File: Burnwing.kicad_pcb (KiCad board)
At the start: 2 copper layers, 50.8 x 22.9 mm, 61 parts, among them J1 Conn_01x06_MountingPin, J2 PinHeader_1x02_P1.00mm_Vertic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, Q1 AONR21307, Q2 NCV8402ADDR2G, X1 USB Type C, X2 HUSB238

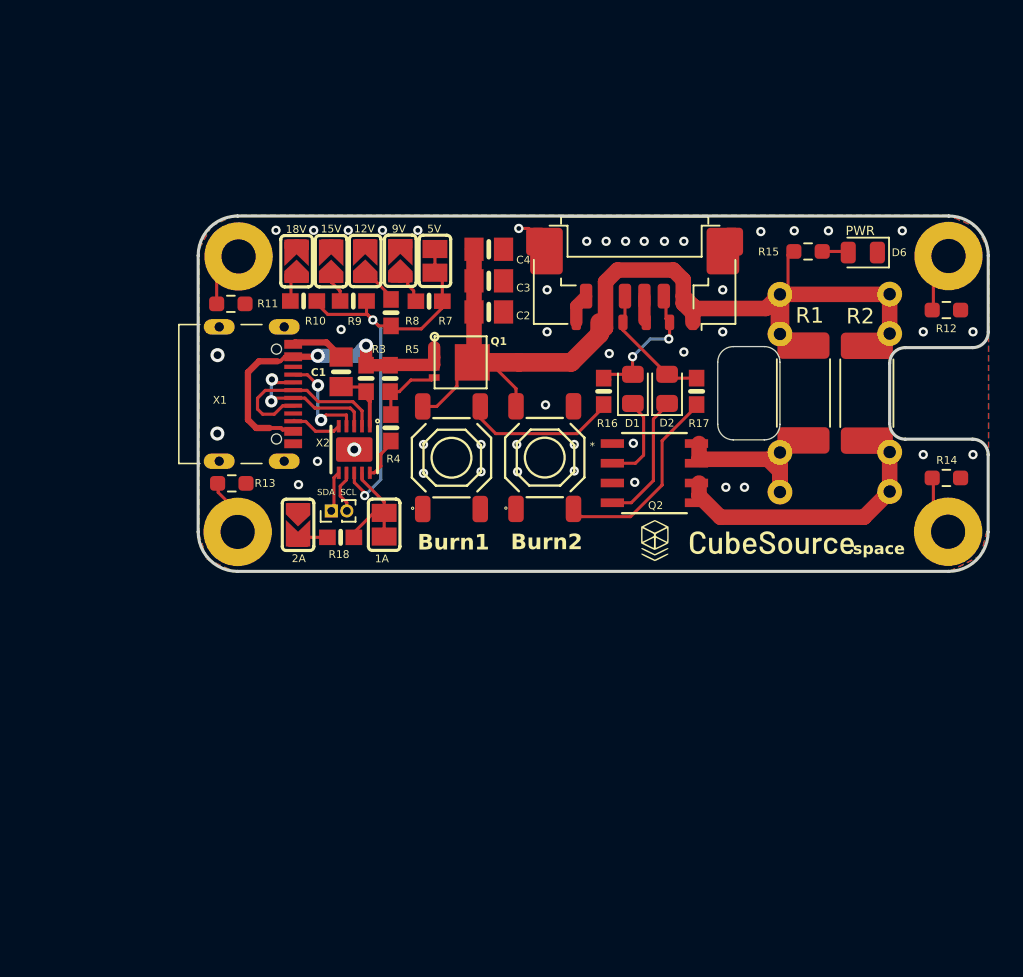
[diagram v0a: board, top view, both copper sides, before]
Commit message: Reworked the layout
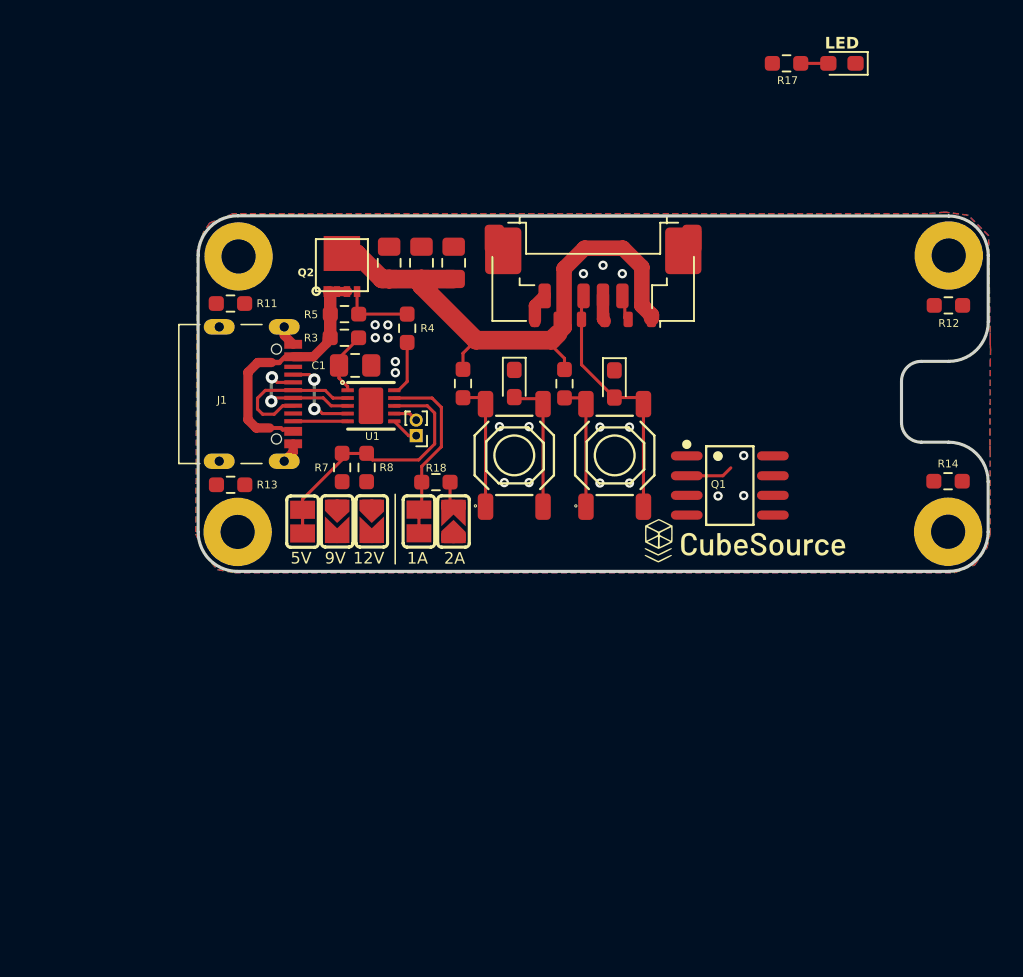
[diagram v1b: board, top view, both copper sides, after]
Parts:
- removed 15V, 18V: , Library:SOLDERJUMPER_ARROW_NOPASTE
- removed D6: LED_RED_IN1, Library:LED_0805_2012Metric
- removed H2: MountingHole_Pad, Library:MountingHole_2.2mm_M2_Pad
- removed the Q2 at (106.9, 96.6)
- removed R1: 4.7, Library:AxialBurnResistor
- removed R16: 510, Library:0603-NO
- removed the R17 at (109.6, 91.3)
- removed R2: 4.7, Library:AxialBurnResistor_No_Cutout
- removed REF** (x2): R_2512_6332Metric_Pad1.40x3.35mm_HandSolder, Library:R_2512_6332Metric_Pad1.40x3.35mm_HandSolder
- added ?: MountingHole_2.2mm_M2_Pad, MountingHole:MountingHole_2.2mm_M2_Pad, F.Cu at (125.8, 82.6)
- added D3: LED, LED_SMD:LED_0603_1608Metric_Pad1.05x0.95mm_HandSolder, F.Cu at (119.0, 70.2)
- added Q1: NCV8402ADDR2G, EasyEDA:SOIC-8_L4.9-W3.9-P1.27-LS6.0-BL, F.Cu at (111.8, 97.4)
- Burn1, Burn2: footprint Library:SW-SMD_4P-L5.1-W5.1-P3.70-LS6.5-TL-2 -> PCM_JLCPCB:SW-SMD_4P-L5.1-W5.1-P3.70-LS6.5-TL-2
- C1, C2, C3, C4: footprint Library:0805-NO -> Capacitor_SMD:C_0805_2012Metric_Pad1.18x1.45mm_HandSolder
- D1: value LED_RED_IN1 -> LED; footprint Library:LED_0805_2012Metric -> LED_SMD:LED_0603_1608Metric_Pad1.05x0.95mm_HandSolder
- D2: value LED_RED_IN2 -> LED; footprint Library:LED_0805_2012Metric -> LED_SMD:LED_0603_1608Metric_Pad1.05x0.95mm_HandSolder
- H1, H3, H4: footprint Library:MountingHole_2.2mm_M2_Pad -> MountingHole:MountingHole_2.2mm_M2_Pad
- J2: renamed from J1; footprint Library:Molex_PicoBlade_53261-0671_1x06-1MP_P1.25mm_Horizontal -> Connector_Molex:Molex_PicoBlade_53261-0671_1x06-1MP_P1.25mm_Horizontal
- J3: renamed from J2; value PinHeader_1x02_P1.00mm_Vertical -> Conn_01x02_Pin; footprint Library:PinHeader_1x02_P1.00mm_Vertical -> Connector_PinHeader_1.00mm:PinHeader_1x02_P1.00mm_Vertical
- R10: value 18K -> 750; footprint Library:0603-NO -> Resistor_SMD:R_0603_1608Metric_Pad0.98x0.95mm_HandSolder
- R11, R12, R13, R14: footprint Library:R_0603_1608Metric_Pad0.98x0.95mm_HandSolder -> Resistor_SMD:R_0603_1608Metric_Pad0.98x0.95mm_HandSolder
- R17: renamed from R15; value 750 -> 5.1K; footprint Library:R_0603_1608Metric_Pad0.98x0.95mm_HandSolder -> Resistor_SMD:R_0603_1608Metric_Pad0.98x0.95mm_HandSolder
- R18, R4, R5, R7, R8: footprint Library:0603-NO -> Resistor_SMD:R_0603_1608Metric_Pad0.98x0.95mm_HandSolder
- R3: value 10 ohm -> 10; footprint Library:0603-NO -> Resistor_SMD:R_0603_1608Metric_Pad0.98x0.95mm_HandSolder
- R9: value 14K -> 750; footprint Library:0603-NO -> Resistor_SMD:R_0603_1608Metric_Pad0.98x0.95mm_HandSolder
- moved 5V 18.8 mm to (84.3, 99.7), turned to -90 degrees
- moved R10 17.6 mm to (101.1, 90.8), turned to -90 degrees
- moved 9V 17.3 mm to (86.5, 99.7), turned to -90 degrees
- moved 12V 16.8 mm to (88.7, 99.7), turned to -90 degrees
- moved R17 12.2 mm to (115.4, 70.2)
- moved R7 12.1 mm to (86.8, 96.2), turned to 90 degrees
- moved R8 10.1 mm to (88.4, 96.2), turned to 90 degrees
- moved 2A 10.0 mm to (94.0, 99.7), turned to 90 degrees
- moved D2 9.84 mm to (97.9, 90.8), turned to -90 degrees
- moved Q2 9.51 mm to (86.8, 83.5), turned to 90 degrees
- moved R9 8.83 mm to (94.6, 90.8), turned to -90 degrees
- moved J3 7.30 mm to (91.6, 94.2), turned to 180 degrees
- moved R18 7.08 mm to (92.8, 97.2), turned to 180 degrees
- moved R4 6.49 mm to (91.0, 87.3)
- moved C4 6.47 mm to (89.8, 83.1), turned to 90 degrees
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- renumbered X1 to J1, Q1 to Q2, X2 to U1
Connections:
- net CC1 renamed /CC1
- net CC2 renamed /CC2
- net D+ renamed /D+
- net D- renamed /D-
- net SCL renamed /SCL
- net SDA renamed /SDA
- net VBUS renamed /VBUS
- 5V pad 1: N$3 -> Net-(U1-VSET)
- Burn1 pad 1: (no net) -> Net-(Burn1-B)
- Burn1 pad 2: VOUT -> Net-(Burn1-B)
- Burn1 pad 3: (no net) -> BURN_CTRL_1
- Burn2 pad 1: (no net) -> Net-(Burn2-B)
- Burn2 pad 2: VOUT -> Net-(Burn2-B)
- Burn2 pad 4: (no net) -> BURN_CTRL_2
- C2 pad 1: VOUT -> VDC
- C3 pad 1: VOUT -> VDC
- C4 pad 1: VOUT -> VDC
- D1 pad 1: /GATE1 -> Net-(D1-K)
- D1 pad 2: BURN_CTRL_1 -> BURN_CTRL_2
- D2 pad 1: /GATE2 -> GND
- D2 pad 2: BURN_CTRL_2 -> BURN_CTRL_1
- J1 pad A8: (no net) -> unconnected-(J1-SBU1-PadA8)
- J1 pad B8: (no net) -> unconnected-(J1-SBU2-PadB8)
- J2 pad 1: VOUT -> VDC
- J2 pad 5: VOUT -> VDC
- Q2 pad 5678: VOUT -> VDC
- R10 pad 1: N$8 -> VDC
- R10 pad 2: N$3 -> Net-(Burn2-B)
- R12 pad 1: Net-(H2-Pad1) -> Net-(H3-Pad1)
- R13 pad 1: Net-(H3-Pad1) -> Net-(H2-Pad1)
- R17 pad 1: VOUT -> VDC
- R17 pad 2: VOUT -> Net-(D3-A)
- R7 pad 2: N$3 -> Net-(U1-VSET)
- R8 pad 2: N$3 -> Net-(U1-VSET)
- R9 pad 1: N$7 -> VDC
- R9 pad 2: N$3 -> Net-(Burn1-B)
- U1 pad 8: N$3 -> Net-(U1-VSET)
- p pad 1: VOUT -> VDC
- p pad 5: VOUT -> VDC
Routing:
- net VOUT: track 66.2 -> 0.00 mm
- net VDC: track 0.00 -> 40.8 mm
- net N$3: track 26.9 -> 0.00 mm, vias 2 -> 0
- net Net-(R2-Pad2): track 16.9 -> 0.00 mm
- net Net-(U1-VSET): track 0.00 -> 16.1 mm
- net Net-(R1-Pad2): track 14.0 -> 0.00 mm
- net /GATE2: track 8.56 -> 0.00 mm
- net Net-(Burn1-B): track 0.00 -> 8.39 mm
- net Net-(Burn2-B): track 0.00 -> 8.15 mm
- net BURN_CTRL_1: track 19.9 -> 12.5 mm, vias 2 -> 0
- net /GATE1: track 5.83 -> 0.00 mm
- net BURN_CTRL_2: track 20.9 -> 16.1 mm
- net Net-(U1-ISET): track 5.70 -> 10.5 mm
- net Net-(H3-Pad1): track 4.63 -> 0.00 mm
- net /VBUS: track 21.6 -> 17.0 mm, vias 2 -> 0
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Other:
- outline, holes or cut-outs redrawn
- board text removed: "PWR"

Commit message: Layout completed
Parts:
- removed ?: MountingHole_2.2mm_M2_Pad, MountingHole:MountingHole_2.2mm_M2_Pad
- added H2: MountingHole_Pad, MountingHole:MountingHole_2.2mm_M2_Pad, F.Cu at (125.8, 82.6)
- added R1: 4.7, Library:AxialBurnResistor, F.Cu at (116.4, 91.4)
- added R2: 4.7, Library:AxialBurnResistor_No_Cutout, F.Cu at (123.4, 91.4)
- added REF**: R_2512_6332Metric_Pad1.40x3.35mm_HandSolder, Library:R_2512_6332Metric_Pad1.40x3.35mm_HandSolder, F.Cu at (122.0, 91.4)
- added REF**: R_2512_6332Metric_Pad1.40x3.35mm_HandSolder, Library:R_2512_6332Metric_Pad1.40x3.35mm_HandSolder, F.Cu at (118.1, 91.4)
- D3: value LED -> PWR
- moved D3 12.4 mm to (121.0, 82.5)
- moved R17 12.4 mm to (117.5, 82.5)
- moved Q1 4.95 mm to (109.7, 92.9), turned to 180 degrees
- moved .space 2.53 mm to (114.8, 100.8)
- moved R12 0.89 mm to (125.8, 86.7), turned to -90 degrees
- moved R7 0.89 mm to (87.7, 96.2)
- moved R8 0.86 mm to (89.2, 96.2)
- moved R14 0.84 mm to (125.8, 96.3), turned to 90 degrees
- moved 1A 0.36 mm to (91.4, 99.7)
- moved Burn1 0.33 mm to (97.6, 95.4)
- moved D2 0.33 mm to (97.6, 90.8)
- moved R9 0.33 mm to (94.3, 90.8)
- moved R18 0.26 mm to (92.6, 97.2)
- moved R10 0.24 mm to (100.9, 90.8)
- moved 5V 0.23 mm to (84.0, 99.7)
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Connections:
- D1 pad 1: Net-(D1-K) -> GND
- R12 pad 1: Net-(H3-Pad1) -> Net-(H2-Pad1)
- R13 pad 1: Net-(H2-Pad1) -> Net-(H3-Pad1)
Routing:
- net BURN_CTRL_1: track 12.5 -> 36.5 mm
- net VDC: track 40.8 -> 64.6 mm
- net Net-(Q1-D2-Pad5): track 0.00 -> 21.6 mm
- net Net-(Q1-D1-Pad7): track 0.00 -> 10.8 mm
- net BURN_CTRL_2: track 16.1 -> 12.5 mm
- net Net-(H2-Pad1): track 0.00 -> 3.16 mm
- net Net-(H4-Pad1): track 0.00 -> 2.97 mm
- net Net-(U1-VSET): track 16.1 -> 14.1 mm
- net Net-(H3-Pad1): track 0.00 -> 1.67 mm
- net Net-(9V1-Pad1): track 0.00 -> 1.65 mm
- net Net-(H1-Pad1): track 0.00 -> 1.59 mm
- net Net-(12V1-Pad1): track 0.00 -> 1.56 mm
- net Net-(Burn1-A): track 8.39 -> 7.29 mm
- net Net-(U1-VIN): track 4.05 -> 3.33 mm
- net Net-(Burn2-A): track 8.15 -> 8.72 mm
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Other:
- outline, holes or cut-outs redrawn

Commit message: Cleaned schematic a bit
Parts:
- renumbered D2 to D1, D1 to D2
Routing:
- net BURN_CTRL_2: track 12.5 -> 11.9 mm
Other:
- outline, holes or cut-outs redrawn

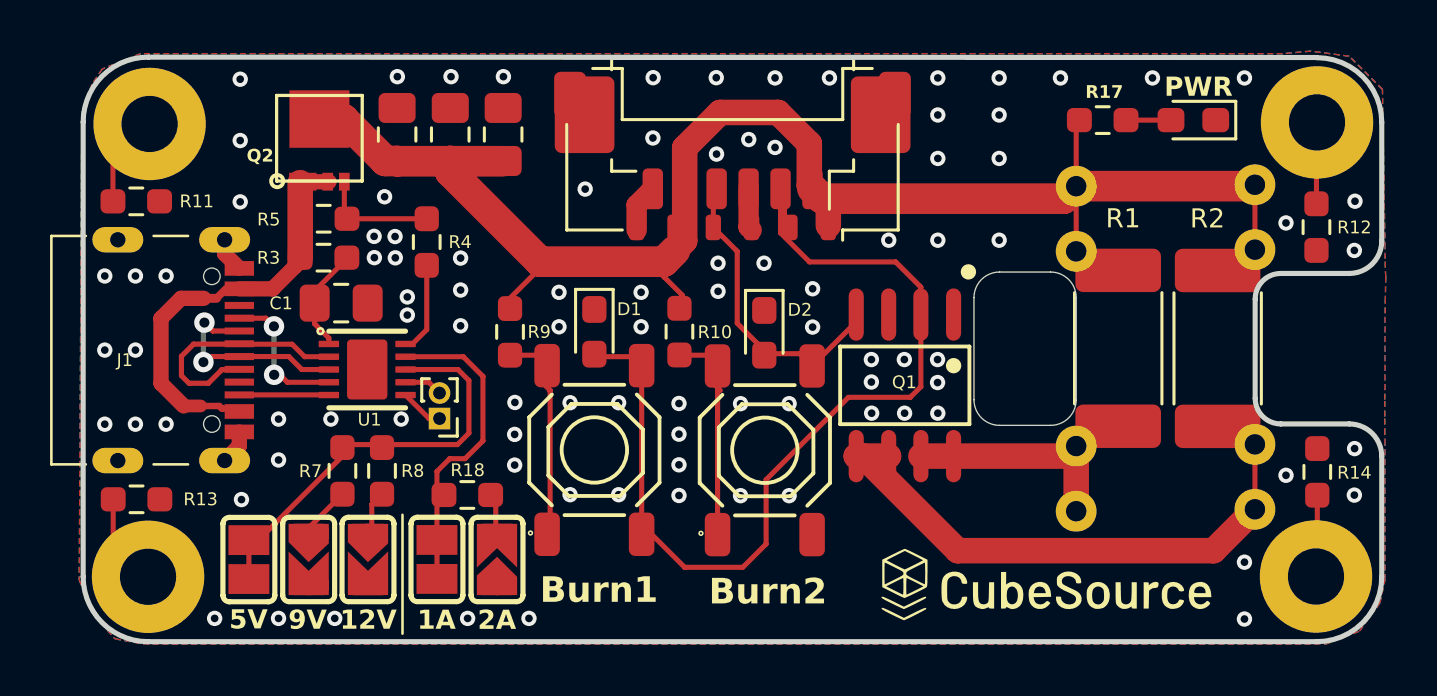
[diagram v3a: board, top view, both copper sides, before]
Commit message: Reworked usb power and cleaned up layout
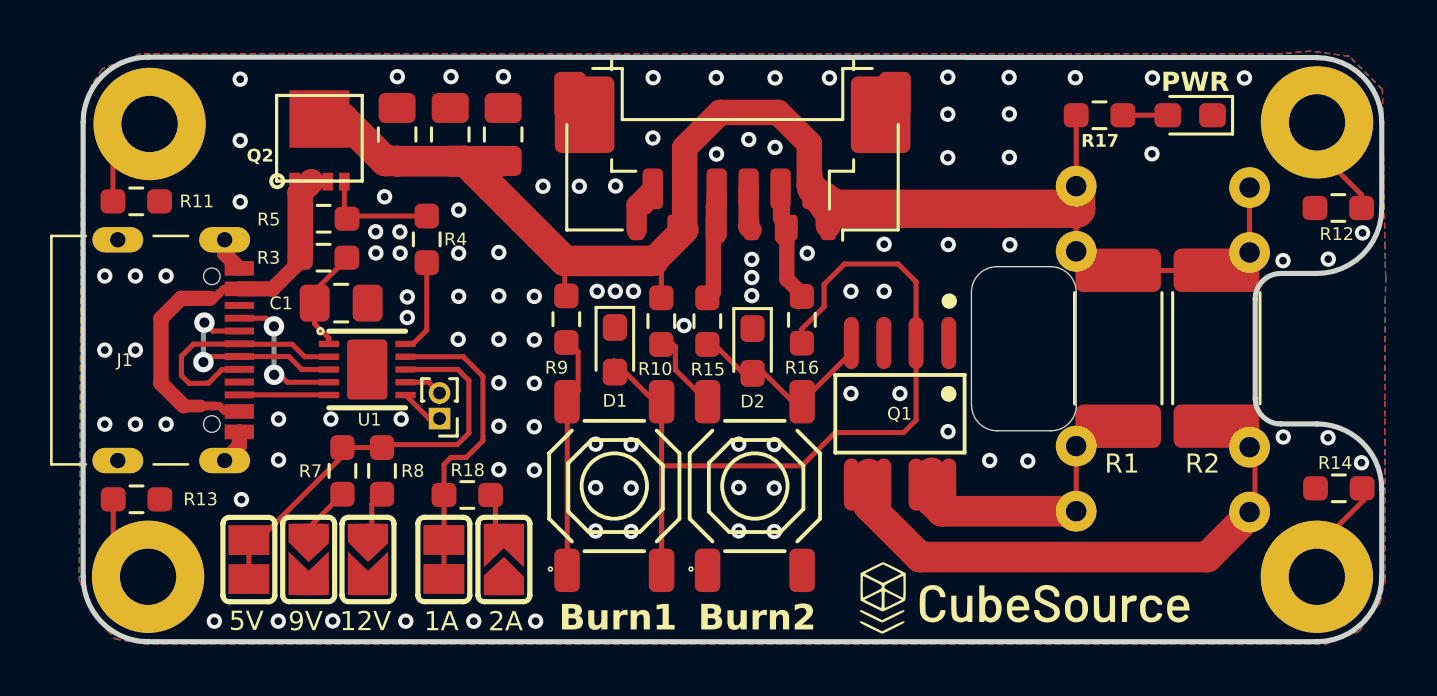
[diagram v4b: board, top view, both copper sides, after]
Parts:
- added R15: 750, R_0603_1608Metric_Pad0.98x0.95mm_HandSolder, F.Cu at (102.0, 90.4)
- added R16: 750, R_0603_1608Metric_Pad0.98x0.95mm_HandSolder, F.Cu at (105.7, 90.3)
- .space: footprint Library:LOGO -> LOGO
- 12V, 2A, 9V: footprint Library:SOLDERJUMPER_ARROW_NOPASTE -> SOLDERJUMPER_ARROW_NOPASTE
- 1A, 5V: footprint Library:SOLDERJUMPER_CLOSEDWIRE -> SOLDERJUMPER_CLOSEDWIRE
- Burn1, Burn2: footprint PCM_JLCPCB:SW-SMD_4P-L5.1-W5.1-P3.70-LS6.5-TL-2 -> SW-SMD_4P-L5.1-W5.1-P3.70-LS6.5-TL-2
- C1, C2, C3, C4: footprint Capacitor_SMD:C_0805_2012Metric_Pad1.18x1.45mm_HandSolder -> C_0805_2012Metric_Pad1.18x1.45mm_HandSolder
- D1, D2, D3: footprint LED_SMD:LED_0603_1608Metric_Pad1.05x0.95mm_HandSolder -> LED_0603_1608Metric_Pad1.05x0.95mm_HandSolder
- H1, H2, H3, H4: footprint MountingHole:MountingHole_2.2mm_M2_Pad -> MountingHole_2.2mm_M2_Pad
- J1: footprint Library:USB_C_CUSB31-CFM2AX-01-X -> USB_C_CUSB31-CFM2AX-01-X
- J2: footprint Connector_Molex:Molex_PicoBlade_53261-0671_1x06-1MP_P1.25mm_Horizontal -> Molex_PicoBlade_53261-0671_1x06-1MP_P1.25mm_Horizontal
- J3: footprint Connector_PinHeader_1.00mm:PinHeader_1x02_P1.00mm_Vertical -> PinHeader_1x02_P1.00mm_Vertical
- PLABEL0: footprint Library:PLABEL0 -> PLABEL0
- PLABEL10: footprint Library:PLABEL10 -> PLABEL10
- PLABEL11: footprint Library:PLABEL11 -> PLABEL11
- PLABEL14: footprint Library:PLABEL14 -> PLABEL14
- PLABEL16: footprint Library:PLABEL16 -> PLABEL16
- PLABEL17: footprint Library:PLABEL17 -> PLABEL17
- PLABEL18: footprint Library:PLABEL18 -> PLABEL18
- PLABEL3: footprint Library:PLABEL3 -> PLABEL3
- PLABEL4: footprint Library:PLABEL4 -> PLABEL4
- PLABEL5: footprint Library:PLABEL5 -> PLABEL5
- PLABEL6: footprint Library:PLABEL6 -> PLABEL6
- PLABEL7: footprint Library:PLABEL7 -> PLABEL7
- PLABEL8: footprint Library:PLABEL8 -> PLABEL8
- PLABEL9: footprint Library:PLABEL9 -> PLABEL9
- Q1: footprint EasyEDA:SOIC-8_L4.9-W3.9-P1.27-LS6.0-BL -> SOIC-8_L4.9-W3.9-P1.27-LS6.0-BL
- Q2: footprint Library:POWERDI3333 -> POWERDI3333
- R1: footprint Library:AxialBurnResistor -> AxialBurnResistor
- R10, R11, R12, R13, R14, R17, R18, R3, R4, R5, R7, R8, R9: footprint Resistor_SMD:R_0603_1608Metric_Pad0.98x0.95mm_HandSolder -> R_0603_1608Metric_Pad0.98x0.95mm_HandSolder
- R2: footprint Library:AxialBurnResistor_No_Cutout -> AxialBurnResistor_No_Cutout
- REF** (x2): footprint Library:R_2512_6332Metric_Pad1.40x3.35mm_HandSolder -> R_2512_6332Metric_Pad1.40x3.35mm_HandSolder
- U1: footprint Library:DFN10_3X3MM -> DFN10_3X3MM
- p: footprint Library:Molex_Pico-Lock_504050-0691_1x06-1MP_P1.50mm_Horizontal -> Molex_Pico-Lock_504050-0691_1x06-1MP_P1.50mm_Horizontal
- moved R9 2.26 mm to (96.5, 90.3)
- moved Burn1 1.61 mm to (98.3, 96.8)
- moved Burn2 1.45 mm to (103.8, 96.8)
- moved R12 1.14 mm to (126.7, 85.9), turned to 180 degrees
- moved Q1 1.13 mm to (109.5, 94.0)
- moved D1 1.07 mm to (98.4, 91.5)
- moved R14 1.06 mm to (126.7, 96.9), turned to 180 degrees
- moved .space 1.00 mm to (114.0, 101.3)
- moved D2 0.85 mm to (103.8, 91.5)
- moved R10 0.82 mm to (100.2, 90.4)
- moved 1A 0.27 mm to (91.7, 99.7)
- moved 2A 0.27 mm to (94.0, 99.7)
- moved R2 0.24 mm to (123.2, 91.5)
- moved D3 0.23 mm to (120.9, 82.3)
- moved R17 0.23 mm to (117.3, 82.3)
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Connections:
- Burn2 pad 1: Net-(Burn2-A) -> (no net)
- Burn2 pad 3: BURN_CTRL_2 -> (no net)
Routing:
- net BURN_CTRL_1: track 36.5 -> 41.9 mm
- net Net-(Burn2-A): track 8.72 -> 3.34 mm
- net VDC: track 64.6 -> 60.3 mm
- net BURN_CTRL_2: track 11.9 -> 14.8 mm
- net GND: track 6.33 -> 9.10 mm, vias 95 -> 105
- net Net-(H4-Pad1): track 2.97 -> 5.34 mm
- net Net-(Burn1-A): track 7.29 -> 9.37 mm
- net Net-(Q1-D1-Pad7): track 10.8 -> 9.48 mm
- net Net-(Q1-D2-Pad5): track 21.6 -> 20.5 mm
- net Net-(H2-Pad1): track 3.16 -> 4.10 mm
- net Net-(2A1-Pad2): track 1.03 -> 1.88 mm
- net /VBUS: track 17.0 -> 17.6 mm
- net Net-(U1-ISET): track 10.5 -> 11.1 mm
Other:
- outline, holes or cut-outs redrawn

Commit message: Make some traces widers and added decals
Increased Trace width near R1 and R2 thru holes.

Also added decals
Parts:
- removed PLABEL10: , PLABEL10
- removed PLABEL11: , PLABEL11
- removed PLABEL14: , PLABEL14
- removed PLABEL16: , PLABEL16
- removed PLABEL17: , PLABEL17
- removed PLABEL18: , PLABEL18
- removed PLABEL3: , PLABEL3
- removed PLABEL5: , PLABEL5
- removed PLABEL6: , PLABEL6
- removed PLABEL7: , PLABEL7
- removed PLABEL8: , PLABEL8
- added .space: LOGO, LOGO, B.Cu at (105.0, 99.5)
- added G***: LOGO, LOGO, F.Cu at (103.0, 91.1)
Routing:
- net VDC: track 60.3 -> 68.3 mm
- net Net-(Q1-D1-Pad7): track 9.48 -> 13.5 mm
- net Net-(Q1-D2-Pad5): track 20.5 -> 24.2 mm
- net GND: vias 105 -> 106
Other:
- board text added: "Burnwing Rev2 2025-07-21"

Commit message: Cleaned up files and added part numbers
Updated Schematics
Updated STEP files
Regenerated Project Libraries
Added Part Numbers
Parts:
- removed PLABEL0: , PLABEL0
- removed PLABEL4: , PLABEL4
- removed PLABEL9: , PLABEL9
- .space (x2), G***: footprint LOGO -> Library:LOGO
- 12V, 2A, 9V: footprint SOLDERJUMPER_ARROW_NOPASTE -> Library:SOLDERJUMPER_ARROW_NOPASTE
- 1A, 5V: footprint SOLDERJUMPER_CLOSEDWIRE -> Library:SOLDERJUMPER_CLOSEDWIRE
- Burn1, Burn2: footprint SW-SMD_4P-L5.1-W5.1-P3.70-LS6.5-TL-2 -> Library:SW-SMD_4P-L5.1-W5.1-P3.70-LS6.5-TL-2
- C1, C2, C3, C4: footprint C_0805_2012Metric_Pad1.18x1.45mm_HandSolder -> Library:C_0805_2012Metric_Pad1.18x1.45mm_HandSolder
- D1, D2, D3: footprint LED_0603_1608Metric_Pad1.05x0.95mm_HandSolder -> Library:LED_0603_1608Metric_Pad1.05x0.95mm_HandSolder
- H1, H2, H3, H4: footprint MountingHole_2.2mm_M2_Pad -> Library:MountingHole_2.2mm_M2_Pad
- J1: footprint USB_C_CUSB31-CFM2AX-01-X -> Library:USB_C_CUSB31-CFM2AX-01-X
- J2: footprint Molex_PicoBlade_53261-0671_1x06-1MP_P1.25mm_Horizontal -> Library:Molex_PicoBlade_53261-0671_1x06-1MP_P1.25mm_Horizontal
- J2: renamed from p; footprint Molex_Pico-Lock_504050-0691_1x06-1MP_P1.50mm_Horizontal -> Library:Molex_Pico-Lock_504050-0691_1x06-1MP_P1.50mm_Horizontal
- J3: footprint PinHeader_1x02_P1.00mm_Vertical -> Library:PinHeader_1x02_P1.00mm_Vertical
- Q1: footprint SOIC-8_L4.9-W3.9-P1.27-LS6.0-BL -> Library:SOIC-8_L4.9-W3.9-P1.27-LS6.0-BL
- Q2: footprint POWERDI3333 -> Library:POWERDI3333
- R1: footprint AxialBurnResistor -> Library:AxialBurnResistor
- R10, R11, R12, R13, R14, R15, R16, R17, R18, R3, R4, R5, R7, R8, R9: footprint R_0603_1608Metric_Pad0.98x0.95mm_HandSolder -> Library:R_0603_1608Metric_Pad0.98x0.95mm_HandSolder
- R2: footprint AxialBurnResistor_No_Cutout -> Library:AxialBurnResistor_No_Cutout
- REF** (x2): footprint R_2512_6332Metric_Pad1.40x3.35mm_HandSolder -> Library:R_2512_6332Metric_Pad1.40x3.35mm_HandSolder
- U1: footprint DFN10_3X3MM -> Library:DFN10_3X3MM
